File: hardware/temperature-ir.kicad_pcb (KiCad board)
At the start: 2 copper layers, 20 x 25 mm, 23 parts, among them P1 CON-SENSOR2, P2 DEBUG, P3 BOOT, U1 XMC1XXX24, U2 MLX90614, U4 DRILL, U5 DRILL, U6 DRILL, U7 DRILL

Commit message: Place CE & WEEE logo
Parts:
- moved VAL 52.9 mm to (119.8, 104.3)
- moved VAL 41.7 mm to (126.3, 104.3)
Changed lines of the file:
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@@
   )
   (setup
-    (last_trace_width 0.3)
+    (last_trace_width 0.24892)
     (user_trace_width 0.2)
     (user_trace_width 0.25)
@@
   )
   (module kicad-libraries:CE_5mm (layer Rückseite)
-    (at 169.38 122.76 180)
+    (at 119.83 104.31 180)
     (fp_text reference VAL (at 0 0 180) (layer B.SilkS) hide
       (effects (font (size 0.2 0.2) (thickness 0.05)) (justify mirror))
@@
   )
   (module kicad-libraries:WEEE_7mm (layer Rückseite)
-    (at 156.28 133.26 180)
+    (at 126.28 104.31 180)
     (fp_text reference VAL (at 0 0 180) (layer B.SilkS) hide
       (effects (font (size 0.2 0.2) (thickness 0.05)) (justify mirror))
@@
   (segment (start 114.805 106.785) (end 116.201447 106.785) (width 0.25) (layer Vorderseite) (net 11))
   (segment (start 116.201447 106.785) (end 117.271332 105.715115) (width 0.25) (layer Vorderseite) (net 11))
-  (segment (start 120.526447 102.46) (end 120.135115 102.851332) (width 0.25) (layer Vorderseite) (net 12) (status 800000))
+  (segment (start 120.526447 102.46) (end 120.135115 102.851332) (width 0.25) (layer Vorderseite) (net 12))
   (segment (start 125.28 102.46) (end 120.526447 102.46) (width 0.25) (layer Vorderseite) (net 12))
   (segment (start 125.78 101.96) (end 125.28 102.46) (width 0.25) (layer Vorderseite) (net 12))

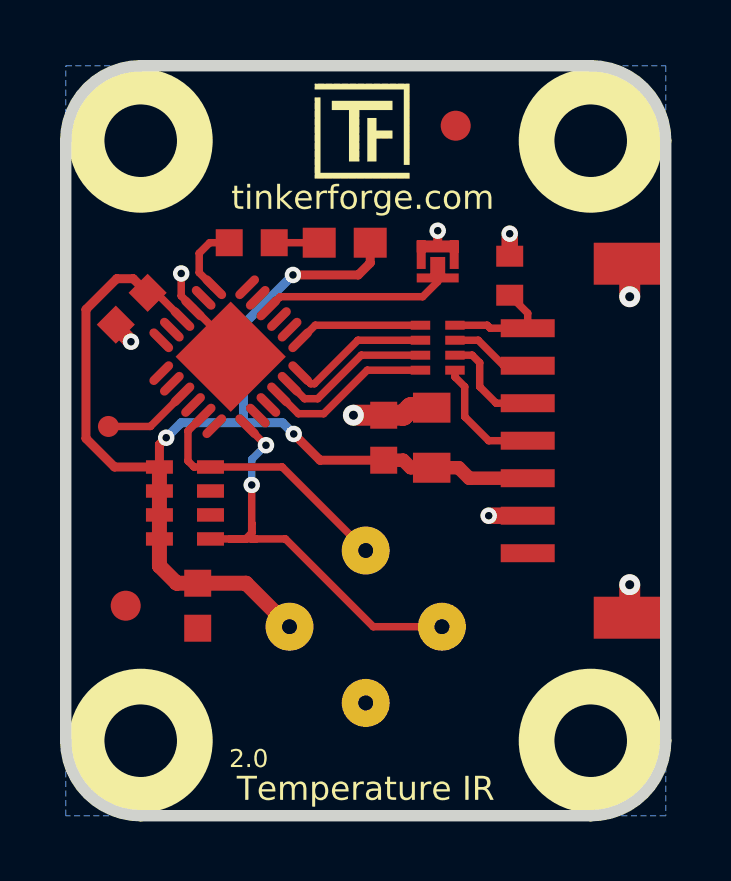
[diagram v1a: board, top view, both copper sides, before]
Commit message: Add missing GND via, fix BootPad
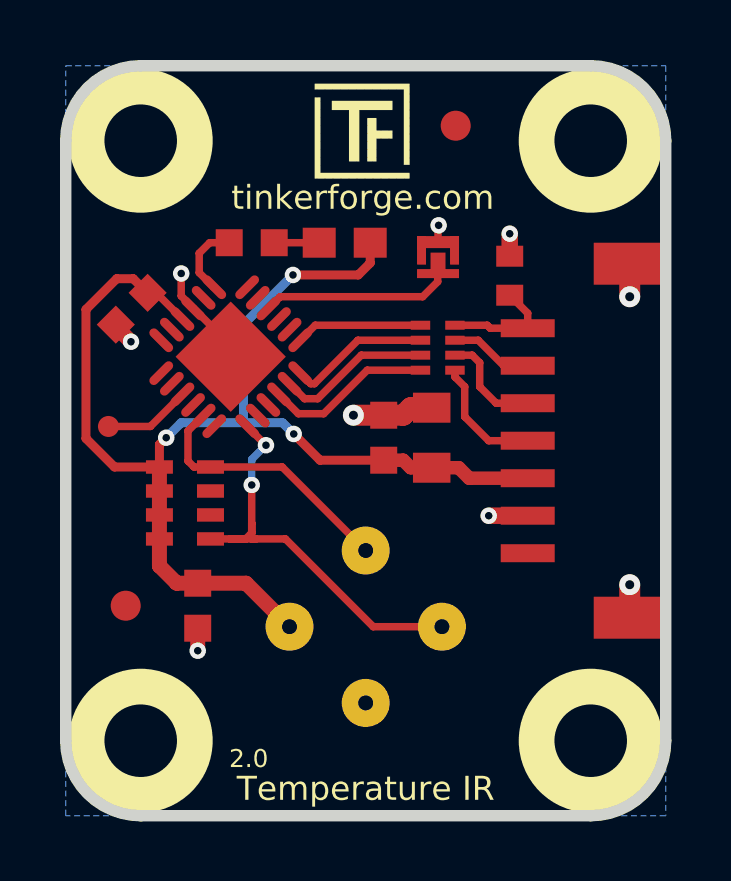
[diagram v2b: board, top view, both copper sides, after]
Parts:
- moved P3 0.15 mm to (125.8, 101.1)
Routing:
- net GND: track 16.7 -> 19.1 mm, vias 8 -> 9
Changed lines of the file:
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@@
   (general
     (links 45)
-    (no_connects 4)
-    (area 113.189499 94.569499 133.570501 119.950501)
+    (no_connects 0)
+    (area 112.494659 93.874659 284.075862 165.350743)
     (thickness 1.6002)
     (drawings 12)
-    (tracks 141)
+    (tracks 154)
     (zones 0)
     (modules 23)
@@
   (layers
     (0 Vorderseite signal)
-    (31 Rückseite signal)
+    (31 Rückseite signal hide)
     (32 B.Adhes user)
     (33 F.Adhes user)
     (34 B.Paste user)
     (35 F.Paste user)
-    (36 B.SilkS user)
+    (36 B.SilkS user hide)
     (37 F.SilkS user)
     (38 B.Mask user)
@@
   )
   (setup
-    (last_trace_width 0.24892)
+    (last_trace_width 0.25)
     (user_trace_width 0.2)
     (user_trace_width 0.25)
@@
   )
   (module kicad-libraries:SolderJumper (layer Vorderseite)
-    (at 125.78 101.285 270)
+    (at 125.79 101.14 270)
     (fp_text reference P3 (at 0 0.2 270) (layer F.Fab)
       (effects (font (size 0.3 0.3) (thickness 0.0712)))
@@
     (effects (font (size 0.8001 0.8001) (thickness 0.14986)))
   )
-  (segment (start 125.78 100.785) (end 125.78 100.26) (width 0.3) (layer Vorderseite) (net 1))
-  (via (at 125.78 100.26) (size 0.55) (drill 0.25) (layers Vorderseite Rückseite) (net 1))
+  (segment (start 125.79 100.64) (end 125.79 100.1) (width 0.25) (layer Vorderseite) (net 1))
+  (via (at 125.81 100.08) (size 0.55) (drill 0.25) (layers Vorderseite Rückseite) (net 1))
+  (segment (start 125.79 100.1) (end 125.81 100.08) (width 0.25) (layer Vorderseite) (net 1))
+  (segment (start 126.34 100.915) (end 126.34 100.72) (width 0.25) (layer Vorderseite) (net 1))
+  (segment (start 126.34 100.72) (end 126.28 100.66) (width 0.25) (layer Vorderseite) (net 1))
+  (segment (start 126.28 100.66) (end 125.81 100.66) (width 0.25) (layer Vorderseite) (net 1))
+  (segment (start 125.81 100.66) (end 125.79 100.64) (width 0.25) (layer Vorderseite) (net 1))
+  (segment (start 125.24 100.915) (end 125.24 100.73) (width 0.25) (layer Vorderseite) (net 1))
+  (segment (start 125.24 100.73) (end 125.32 100.65) (width 0.25) (layer Vorderseite) (net 1))
+  (segment (start 125.32 100.65) (end 125.82 100.65) (width 0.25) (layer Vorderseite) (net 1))
+  (segment (start 125.82 100.65) (end 125.79 100.64) (width 0.25) (layer Vorderseite) (net 1))
+  (segment (start 117.78 113.51) (end 117.78 114.26) (width 0.5) (layer Vorderseite) (net 1))
+  (via (at 117.78 114.26) (size 0.55) (drill 0.25) (layers Vorderseite Rückseite) (net 1))
   (segment (start 115.04967 103.39033) (end 115.04967 103.45467) (width 0.5) (layer Vorderseite) (net 1))
   (segment (start 115.04967 103.45467) (end 115.555 103.96) (width 0.5) (layer Vorderseite) (net 1))
@@
   (segment (start 114.805 106.785) (end 116.201447 106.785) (width 0.25) (layer Vorderseite) (net 11))
   (segment (start 116.201447 106.785) (end 117.271332 105.715115) (width 0.25) (layer Vorderseite) (net 11))
+  (segment (start 125.79 101.69) (end 125.79 101.27) (width 0.25) (layer Vorderseite) (net 12))
+  (segment (start 125.79 101.27) (end 125.79 101.29) (width 0.25) (layer Vorderseite) (net 12))
   (segment (start 120.526447 102.46) (end 120.135115 102.851332) (width 0.25) (layer Vorderseite) (net 12))
   (segment (start 125.28 102.46) (end 120.526447 102.46) (width 0.25) (layer Vorderseite) (net 12))

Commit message: Add CoMCU Logo
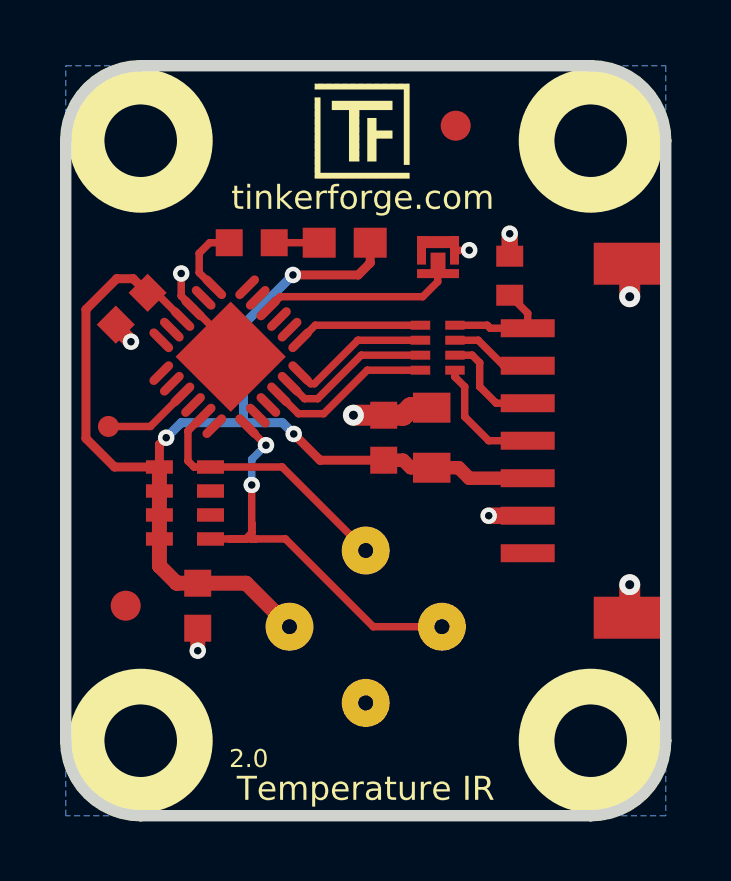
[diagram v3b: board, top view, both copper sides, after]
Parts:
- added G***: LOGO, kicad-libraries:Logo_CoMCU, B.Cu at (123.4, 98.6)
- moved VAL 1.30 mm to (126.3, 105.6)
- moved VAL 0.55 mm to (119.8, 104.9)

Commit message: move sensor to the center
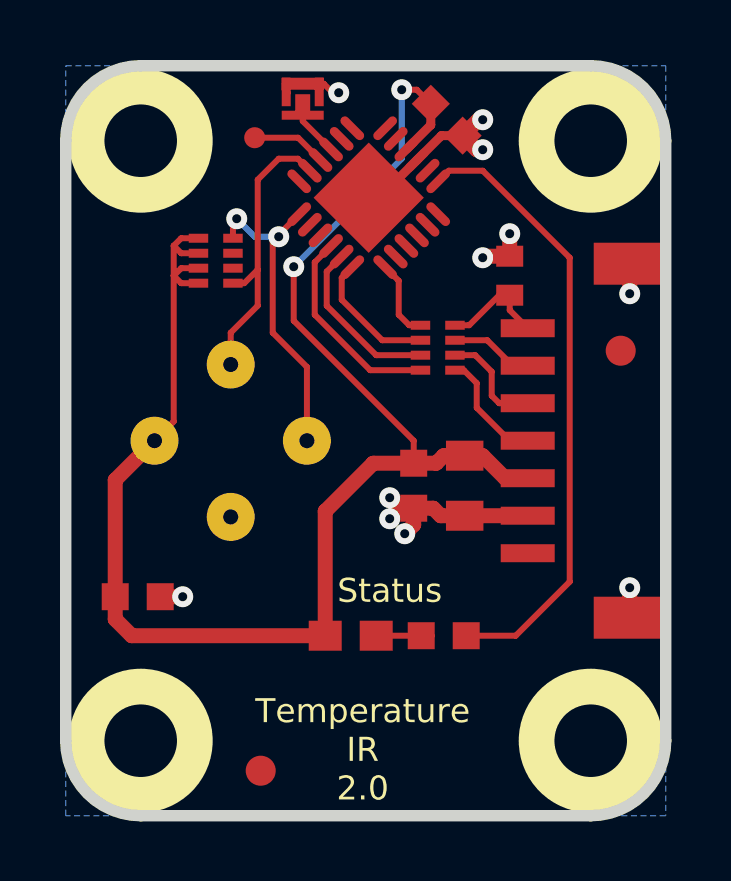
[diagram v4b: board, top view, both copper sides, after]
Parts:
- RP2: footprint kicad-libraries:4X0603 -> kicad-libraries:4X0402
- Ref**: moved to B.Cu
- moved Ref** 18.8 mm to (124.9, 113.9), turned to 180 degrees
- moved R1 14.6 mm to (126.0, 113.8), turned to 180 degrees
- moved D1 13.1 mm to (122.9, 113.8), turned to 0 degrees
- moved C4 12.2 mm to (126.1, 96.6), turned to 315 degrees
- moved VAL 11.5 mm to (128.8, 112.1)
- moved P2 10.8 mm to (119.7, 97.2)
- moved Fiducial_Mark 9.30 mm to (131.9, 104.3)
- moved RP2 8.14 mm to (118.4, 101.3), turned to 270 degrees
- moved U2 7.66 mm to (118.9, 107.3)
- moved Fiducial_Mark 7.11 mm to (119.9, 118.3)
- moved U1 7.02 mm to (123.5, 99.2), turned to 135 degrees
- moved P3 6.94 mm to (121.3, 95.9)
- moved VAL 2.77 mm to (128.9, 104.7)
- moved C5 2.02 mm to (115.8, 112.5), turned to 0 degrees
- moved C1 1.94 mm to (126.7, 108.8), turned to 270 degrees
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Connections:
- P1 pad 1: +5V -> (no net)
- RP2 pad 6: Net-(RP2-Pad6) -> (no net)
- RP2 pad 7: Net-(RP2-Pad7) -> (no net)
- U1 pad 11: Net-(U1-Pad11) -> (no net)
- U1 pad 12: Net-(U1-Pad12) -> (no net)
- U1 pad 13: Net-(U1-Pad13) -> (no net)
- U1 pad 14: Net-(U1-Pad14) -> (no net)
- U1 pad 15: Net-(P2-Pad1) -> Net-(P3-Pad2)
- U1 pad 16: Net-(U1-Pad16) -> Net-(P2-Pad1)
- U1 pad 18: Net-(U1-Pad18) -> (no net)
- U1 pad 2: Net-(U1-Pad2) -> (no net)
- U1 pad 20: Net-(U1-Pad20) -> (no net)
- U1 pad 21: Net-(U1-Pad21) -> (no net)
- U1 pad 3: Net-(U1-Pad3) -> (no net)
- U1 pad 4: Net-(P3-Pad2) -> (no net)
- U1 pad 5: Net-(U1-Pad5) -> (no net)
- U1 pad 6: Net-(U1-Pad6) -> (no net)
- U1 pad 8: Net-(U1-Pad8) -> (no net)
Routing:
- net Net-(R1-Pad1): track 2.50 -> 20.7 mm
- net VCC: track 43.3 -> 54.8 mm, vias 3 -> 2
- net Net-(P3-Pad2): track 6.58 -> 1.93 mm
- net GND: track 19.0 -> 22.7 mm, vias 9 -> 11
- net SCL: track 14.4 -> 10.8 mm
- net S-MISO: track 4.22 -> 2.64 mm
- net S-CS: track 5.58 -> 6.81 mm
- net SDA: track 8.90 -> 9.74 mm
- net Net-(D1-Pad2): track 1.50 -> 2.20 mm
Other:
- net class Default: clearance 0.18034 -> 0.15
- rule trace_clearance: 0.18034 -> 0.15
- board text added: "Status"
- board text added: "Temperature IR 2.0"
- board text removed: "2.0"
- board text removed: "Temperature IR"

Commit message: fix status led text
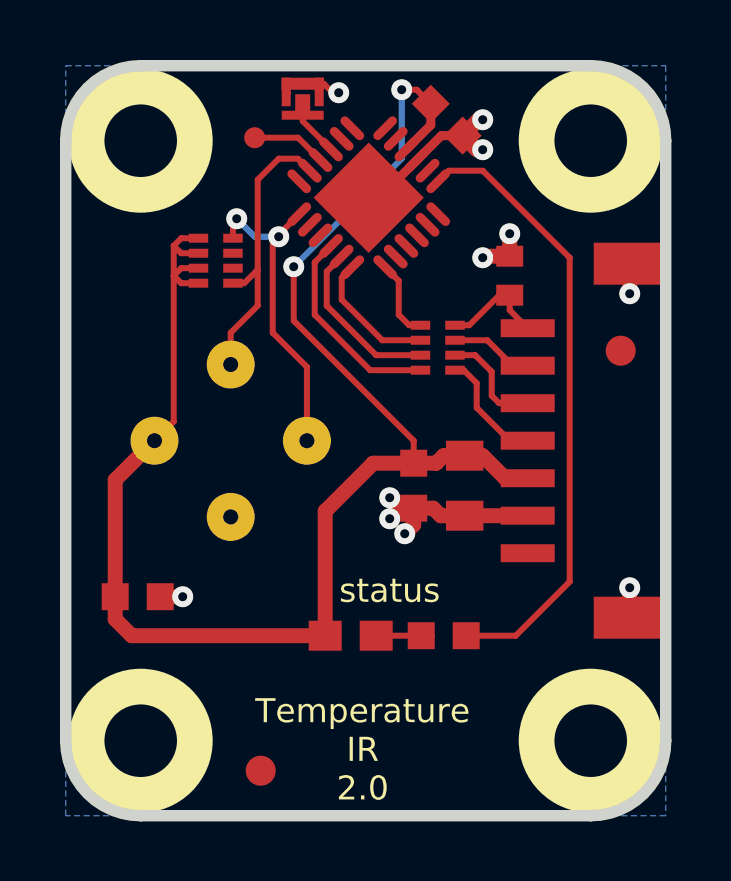
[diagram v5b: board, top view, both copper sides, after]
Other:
- board text added: "status"
- board text removed: "Status"
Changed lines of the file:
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@@
     (links 45)
     (no_connects 0)
-    (area 113.189499 94.569499 133.570501 119.950501)
+    (area 112.524999 93.904999 283.97585 165.750793)
     (thickness 1.6002)
     (drawings 12)
@@
   )
   (setup
-    (last_trace_width 0.2)
+    (last_trace_width 0.24892)
     (user_trace_width 0.2)
     (user_trace_width 0.25)
@@
     )
   )
-  (gr_text Status (at 124.18 112.26) (layer F.SilkS)
+  (gr_text status (at 124.18 112.26) (layer F.SilkS)
     (effects (font (size 0.8001 0.8001) (thickness 0.14986)))
   )

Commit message: specify processor type
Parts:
- U1: value XMC1XXX24 -> XMC110024
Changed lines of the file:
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@@
       (effects (font (size 0.3 0.3) (thickness 0.075)))
     )
-    (fp_text value XMC1XXX24 (at 0 0.8 135) (layer F.Fab)
+    (fp_text value XMC110024 (at 0 0.8 135) (layer F.Fab)
       (effects (font (size 0.3 0.3) (thickness 0.075)))
     )
